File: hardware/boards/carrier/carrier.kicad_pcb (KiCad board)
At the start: 4 copper layers, 81 x 34.3 mm, 52 parts, among them J1 XT30PW(2+2), Q1 IPB020N10N5LF, Q2 2N7002, Q3 2N7002, U1 STM32G031G6U6, U2 LM5163DDAR, U3 LMX5069MS, U4 INA237AIDGSR

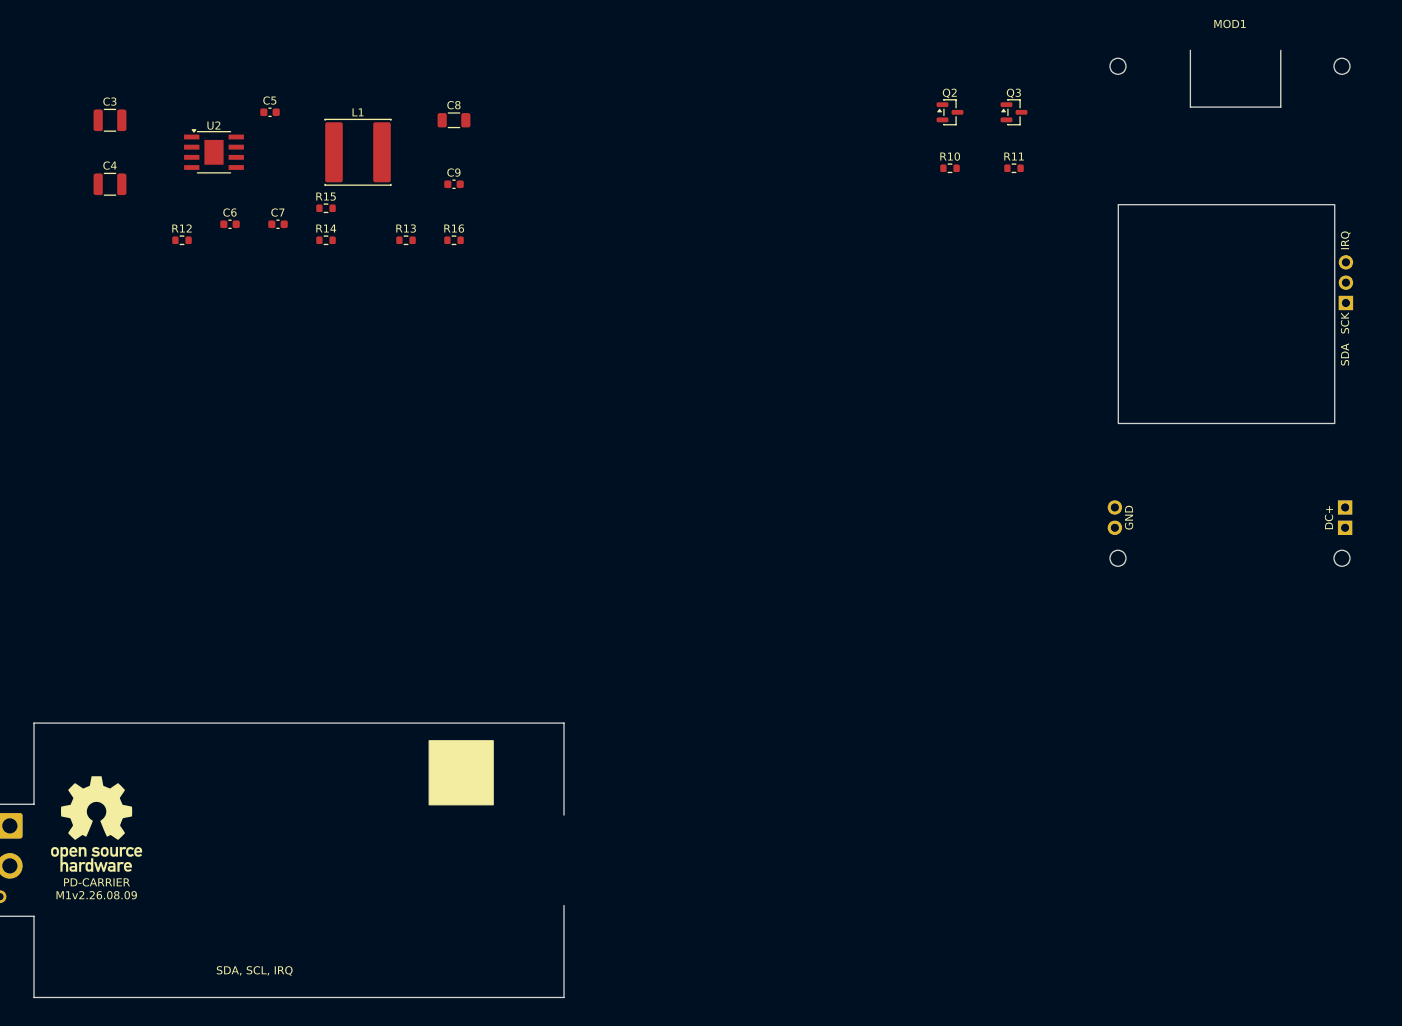
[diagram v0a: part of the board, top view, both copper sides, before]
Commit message: hardware: restore carrier PD module placement
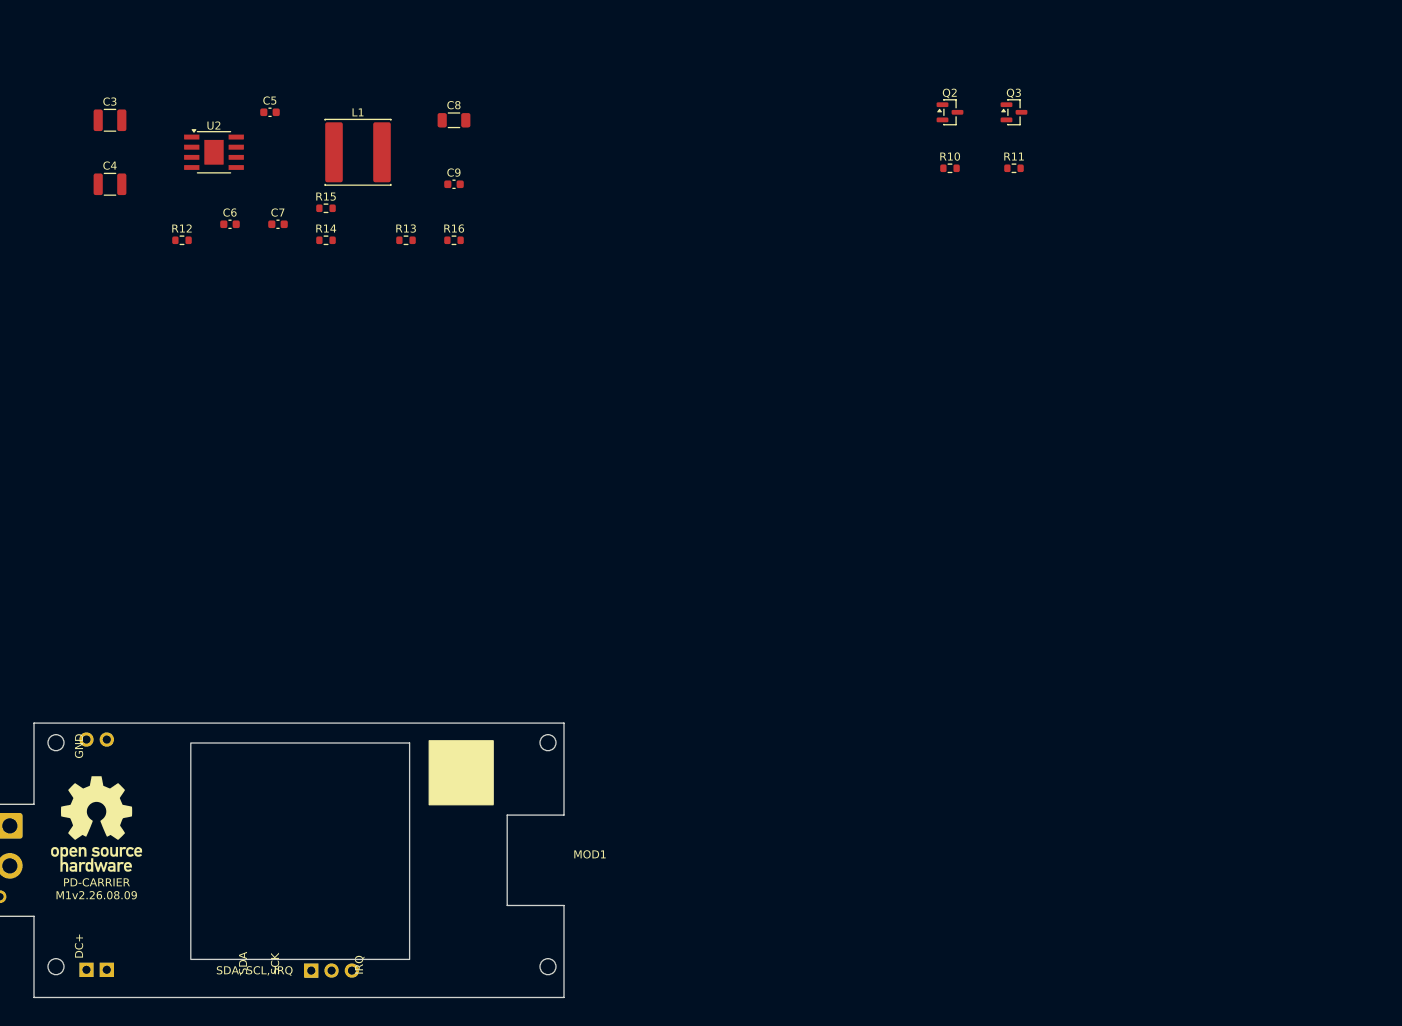
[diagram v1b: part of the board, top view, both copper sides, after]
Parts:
- moved MOD1 134.4 mm to (149.0, 112.8), turned to -90 degrees
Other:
- board text added: "PD ENABLE CONTROL Q2-Q3, R10-R11 - MOD1 on board"
- board text removed: "PD MODULE + ENABLE CONTROL MOD1, Q2-Q3, R10-R11"
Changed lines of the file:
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@@
 	(footprint "mini-rack-power:SW3538_140W_Module"
 		(layer "F.Cu")
-		(at 265 45)
+		(at 149 112.8 -90)
 		(descr "Mechanical/electrical footprint for SW3538 140W USB-C/PD module from hardware/mechanical/exports/SW3538_140W_Module.dxf. Pin placement follows the module holes: GND/DC- column, DC+ column, and side SDA/SCK/IRQ header; verify against module before fabrication.")
 		(tags "SW3538 USB-C PD module 140W daughterboard")
@@
 	)
 	(gr_rect
+		(start 164.9 98.56)
+		(end 172.9 106.56)
+		(stroke
+			(width 0.15)
+			(type solid)
+		)
+		(fill yes)
+		(layer "F.SilkS")
+	)
+	(gr_rect
 		(start 3 10)
 		(end 73 43)
@@
 		(layer "Cmts.User")
 	)
-	(gr_text "INPUT PROTECTION + HOT-SWAP\nD1, U3, Q1, R1-R9, C1-C2"
-		(at 3 8 0)
-		(layer "Cmts.User")
-		(effects
-			(font
-				(size 1.2 1.2)
-				(thickness 0.2)
-				(bold yes)
-			)
-			(justify left bottom)
-		)
-	)
 	(gr_rect
-		(start 121 13)
-		(end 172 40)
+		(start 14 160)
+		(end 44 207)
 		(stroke
 			(width 0.25)
@@
 		(layer "Cmts.User")
 	)
-	(gr_text "3.3 V HOUSEKEEPING BUCK\nU2, L1, C3-C9, R12-R16"
-		(at 121 11 0)
-		(layer "Cmts.User")
-		(effects
-			(font
-				(size 1.2 1.2)
-				(thickness 0.2)
-				(bold yes)
-			)
-			(justify left bottom)
-		)
-	)
 	(gr_rect
-		(start 225 8)
-		(end 284 82)
+		(start 109.8 96.8)
+		(end 125.2 113)
 		(stroke
 			(width 0.25)
@@
 		(layer "Cmts.User")
 	)
-	(gr_text "PD MODULE + ENABLE CONTROL\nMOD1, Q2-Q3, R10-R11"
-		(at 225 6 0)
-		(layer "Cmts.User")
-		(effects
-			(font
-				(size 1.2 1.2)
-				(thickness 0.2)
-				(bold yes)
-			)
-			(justify left bottom)
-		)
-	)
 	(gr_rect
-		(start 330 14)
-		(end 365 36)
+		(start 121 13)
+		(end 172 40)
 		(stroke
 			(width 0.25)
@@
 		(layer "Cmts.User")
 	)
-	(gr_text "POWER / CURRENT MONITOR\nU4, C10, R17-R19"
-		(at 330 12 0)
-		(layer "Cmts.User")
-		(effects
-			(font
-				(size 1.2 1.2)
-				(thickness 0.2)
-				(bold yes)
-			)
-			(justify left bottom)
-		)
-	)
 	(gr_rect
-		(start 14 160)
-		(end 44 207)
+		(start 146 171)
+		(end 154 179)
 		(stroke
 			(width 0.25)
@@
 		(layer "Cmts.User")
 	)
-	(gr_text "MCU + RESET + SWD\nU1, J2, C11-C13, R28, R30"
-		(at 14 158 0)
-		(layer "Cmts.User")
-		(effects
-			(font
-				(size 1.2 1.2)
-				(thickness 0.2)
-				(bold yes)
-			)
-			(justify left bottom)
-		)
-	)
 	(gr_rect
-		(start 146 171)
-		(end 154 179)
+		(start 225 15)
+		(end 242 31)
 		(stroke
 			(width 0.25)
@@
 		(layer "Cmts.User")
 	)
-	(gr_text "BACKPLANE GND TEST\nTP5 - related to J1"
-		(at 146 169 0)
-		(layer "Cmts.User")
-		(effects
-			(font
-				(size 1.2 1.2)
-				(thickness 0.2)
-				(bold yes)
-			)
-			(justify left bottom)
-		)
-	)
 	(gr_rect
 		(start 231 171)
@@
 		(layer "Cmts.User")
 	)
-	(gr_text "OPTIONAL PD I2C PULL-UPS\nR24-R25"
-		(at 231 169 0)
-		(layer "Cmts.User")
-		(effects
-			(font
-				(size 1.2 1.2)
-				(thickness 0.2)
-				(bold yes)
-			)
-			(justify left bottom)
-		)
-	)
 	(gr_rect
-		(start 331 171)
-		(end 347 179)
+		(start 330 14)
+		(end 365 36)
 		(stroke
 			(width 0.25)
@@
 		(layer "Cmts.User")
 	)
-	(gr_text "RGB STATUS LED\nR29, LED1"
-		(at 331 169 0)
-		(layer "Cmts.User")
-		(effects
-			(font
-				(size 1.2 1.2)
-				(thickness 0.2)
-				(bold yes)
-			)
-			(justify left bottom)
-		)
-	)
 	(gr_rect
-		(start 109.8 96.8)
-		(end 125.2 113)
+		(start 331 171)
+		(end 347 179)
 		(stroke
 			(width 0.25)
@@
 		(layer "Cmts.User")
 	)
-	(gr_text "BACKPLANE CONNECTOR\nJ1 - TP5 staged below"
-		(at 126.5 100 0)
-		(layer "Cmts.User")
-		(effects
-			(font
-				(size 1.2 1.2)
-				(thickness 0.2)
-				(bold yes)
-			)
-			(justify left bottom)
-		)
-	)
-	(gr_rect
-		(start 164.9 98.56)
-		(end 172.9 106.56)
-		(stroke
-			(width 0.15)
-			(type solid)
-		)
-		(fill yes)
-		(layer "F.SilkS")
-	)
 	(gr_line
 		(start 100.8 106.5)
@@
 		)
 	)
+	(gr_text "INPUT PROTECTION + HOT-SWAP\nD1, U3, Q1, R1-R9, C1-C2"
+		(at 3 8 0)
+		(layer "Cmts.User")
+		(effects
+			(font
+				(size 1.2 1.2)
+				(thickness 0.2)
+				(bold yes)
+			)
+			(justify left bottom)
+		)
+	)
+	(gr_text "MCU + RESET + SWD\nU1, J2, C11-C13, R28, R30"
+		(at 14 158 0)
+		(layer "Cmts.User")
+		(effects
+			(font
+				(size 1.2 1.2)
+				(thickness 0.2)
+				(bold yes)
+			)
+			(justify left bottom)
+		)
+	)
+	(gr_text "3.3 V HOUSEKEEPING BUCK\nU2, L1, C3-C9, R12-R16"
+		(at 121 11 0)
+		(layer "Cmts.User")
+		(effects
+			(font
+				(size 1.2 1.2)
+				(thickness 0.2)
+				(bold yes)
+			)
+			(justify left bottom)
+		)
+	)
+	(gr_text "BACKPLANE CONNECTOR\nJ1 - TP5 staged below"
+		(at 126.5 100 0)
+		(layer "Cmts.User")
+		(effects
+			(font
+				(size 1.2 1.2)
+				(thickness 0.2)
+				(bold yes)
+			)
+			(justify left bottom)
+		)
+	)
+	(gr_text "BACKPLANE GND TEST\nTP5 - related to J1"
+		(at 146 169 0)
+		(layer "Cmts.User")
+		(effects
+			(font
+				(size 1.2 1.2)
+				(thickness 0.2)
+				(bold yes)
+			)
+			(justify left bottom)
+		)
+	)
+	(gr_text "PD ENABLE CONTROL\nQ2-Q3, R10-R11 - MOD1 on board"
+		(at 225 13 0)
+		(layer "Cmts.User")
+		(effects
+			(font
+				(size 1.2 1.2)
+				(thickness 0.2)
+				(bold yes)
+			)
+			(justify left bottom)
+		)
+	)
+	(gr_text "OPTIONAL PD I2C PULL-UPS\nR24-R25"
+		(at 231 169 0)
+		(layer "Cmts.User")
+		(effects
+			(font
+				(size 1.2 1.2)
+				(thickness 0.2)
+				(bold yes)
+			)
+			(justify left bottom)
+		)
+	)
+	(gr_text "POWER / CURRENT MONITOR\nU4, C10, R17-R19"
+		(at 330 12 0)
+		(layer "Cmts.User")
+		(effects
+			(font
+				(size 1.2 1.2)
+				(thickness 0.2)
+				(bold yes)
+			)
+			(justify left bottom)
+		)
+	)
+	(gr_text "RGB STATUS LED\nR29, LED1"
+		(at 331 169 0)
+		(layer "Cmts.User")
+		(effects
+			(font
+				(size 1.2 1.2)
+				(thickness 0.2)
+				(bold yes)
+			)
+			(justify left bottom)
+		)
+	)

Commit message: checkpoint: carrier layout edits
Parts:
- removed R29: 100R, Resistor_SMD:R_0603_1608Metric
- removed TP5: GND, TestPoint:TestPoint_Pad_D1.0mm
- moved C10 299.9 mm to (43.2, 68.0)
- moved R17 299.9 mm to (38.2, 63.0)
- moved R18 299.9 mm to (38.2, 73.0)
- moved R19 299.9 mm to (63.2, 68.0)
- moved U4 299.9 mm to (53.2, 68.0)
- moved C11 214.8 mm to (222.5, 109.2)
- moved C12 214.8 mm to (244.5, 104.2)
- moved C13 214.8 mm to (244.5, 114.2)
- moved J2 214.8 mm to (234.5, 129.2)
- moved R28 214.8 mm to (222.5, 99.2)
- moved R30 214.8 mm to (244.5, 124.2)
- moved U1 214.8 mm to (234.5, 109.2)
- moved LED1 124.7 mm to (231.3, 119.4)
- moved REF** 86.5 mm to (37.0, 114.6)
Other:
- board text removed: "BACKPLANE CONNECTOR J1 - TP5 staged below"
- board text removed: "BACKPLANE GND TEST TP5 - related to J1"
- board text removed: "RGB STATUS LED R29, LED1"

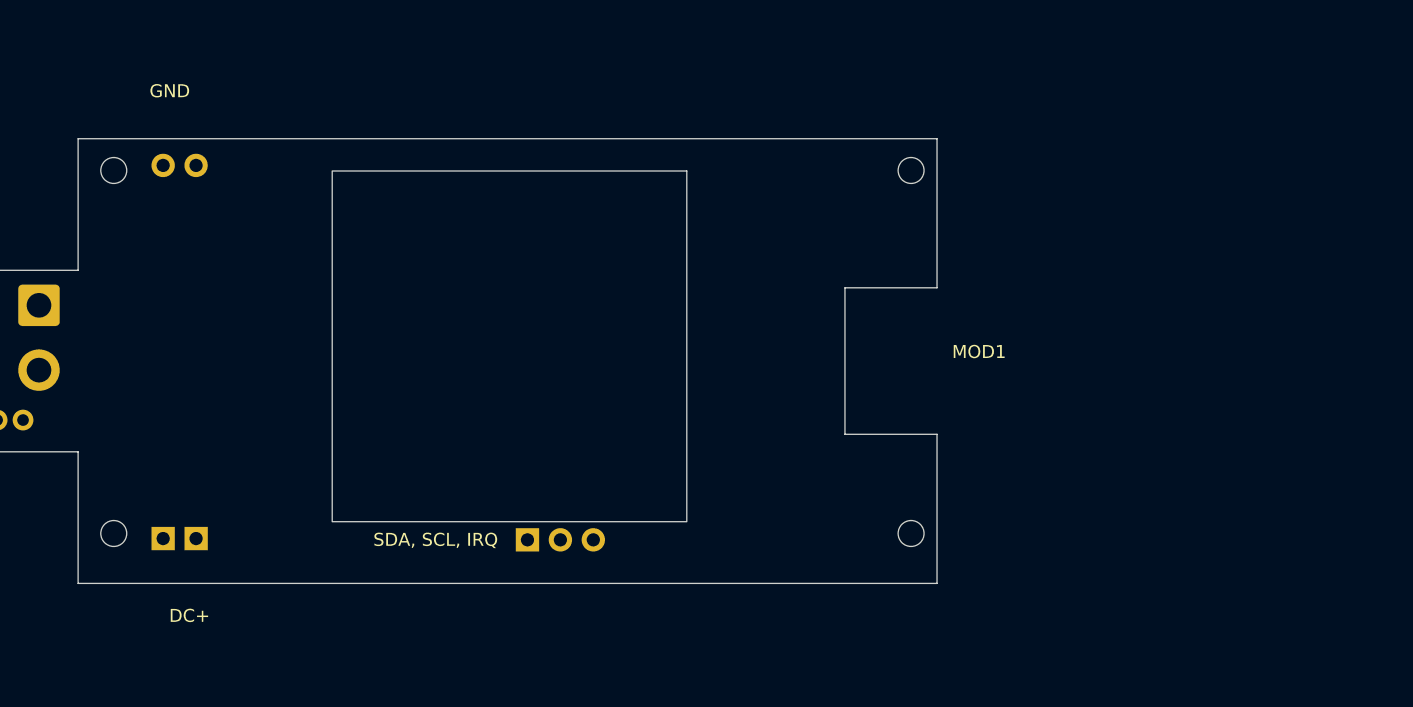
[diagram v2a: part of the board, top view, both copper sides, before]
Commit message: hardware: extend carrier between connectors
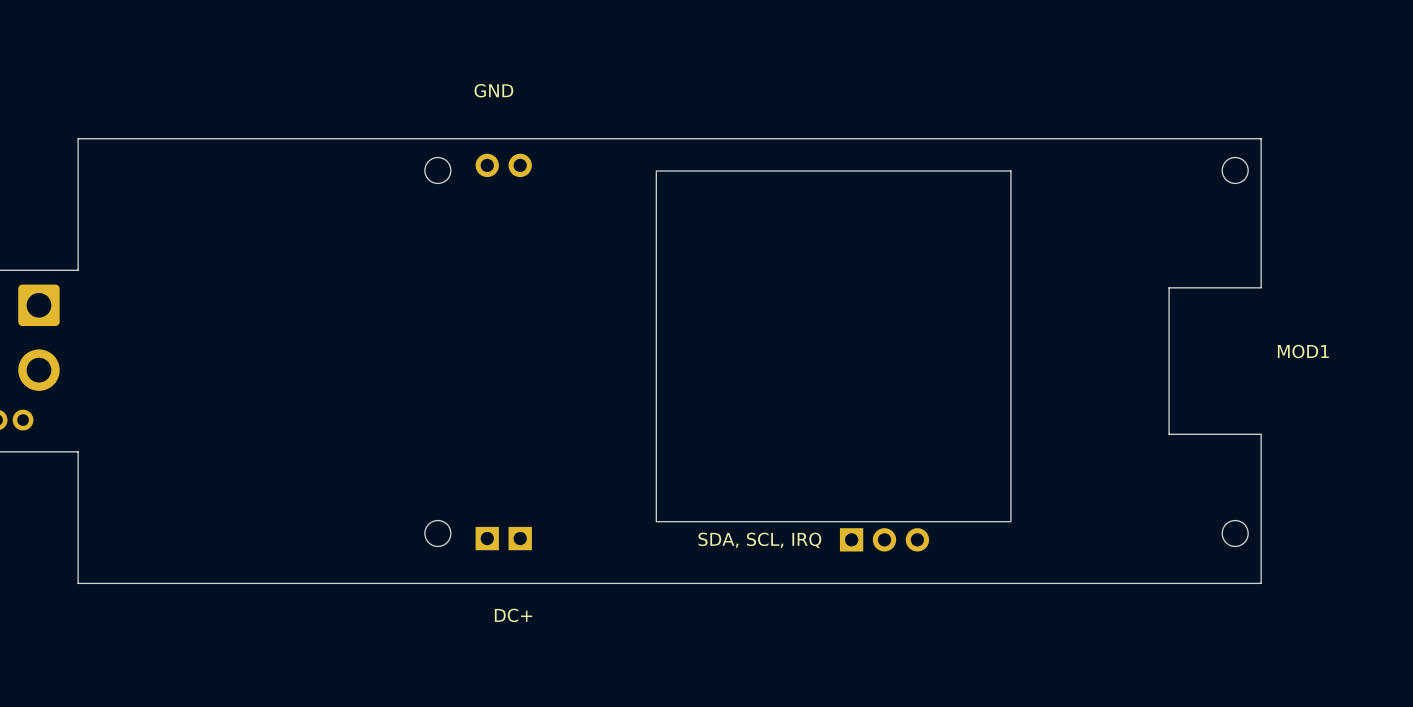
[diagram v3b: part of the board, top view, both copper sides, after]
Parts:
- moved MOD1 25.0 mm to (174.0, 112.8)
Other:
- board size 81 x 34.3 mm -> 106 x 34.3 mm
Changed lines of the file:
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@@
 	(footprint "mini-rack-power:SW3538_140W_Module"
 		(layer "F.Cu")
-		(at 149 112.8 -90)
+		(at 174 112.8 -90)
 		(descr "Mechanical/electrical footprint for SW3538 140W USB-C/PD module from hardware/mechanical/exports/SW3538_140W_Module.dxf. Pin placement follows the module holes: GND/DC- column, DC+ column, and side SDA/SCK/IRQ header; verify against module before fabrication.")
 		(tags "SW3538 USB-C PD module 140W daughterboard")
@@
 	(gr_line
 		(start 115.5 96.35)
-		(end 181.75 96.35)
+		(end 206.75 96.35)
 		(stroke
 			(width 0.05)
@@
 	)
 	(gr_line
-		(start 181.75 96.35)
-		(end 181.75 107.85)
+		(start 206.75 96.35)
+		(end 206.75 107.85)
 		(stroke
 			(width 0.05)
@@
 	)
 	(gr_line
-		(start 181.75 119.15)
-		(end 181.75 130.65)
+		(start 206.75 119.15)
+		(end 206.75 130.65)
 		(stroke
 			(width 0.05)
@@
 	)
 	(gr_line
-		(start 181.75 130.65)
+		(start 206.75 130.65)
 		(end 115.5 130.65)
 		(stroke
@@
 	)
 	(gr_text "SDA, SCL, IRQ"
-		(at 143.08 127.29 0)
+		(at 168.08 127.29 0)
 		(layer "F.SilkS" knockout)
 		(effects
